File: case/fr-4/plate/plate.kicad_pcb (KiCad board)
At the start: 2 copper layers, 152.4 x 104.6 mm, 34 parts

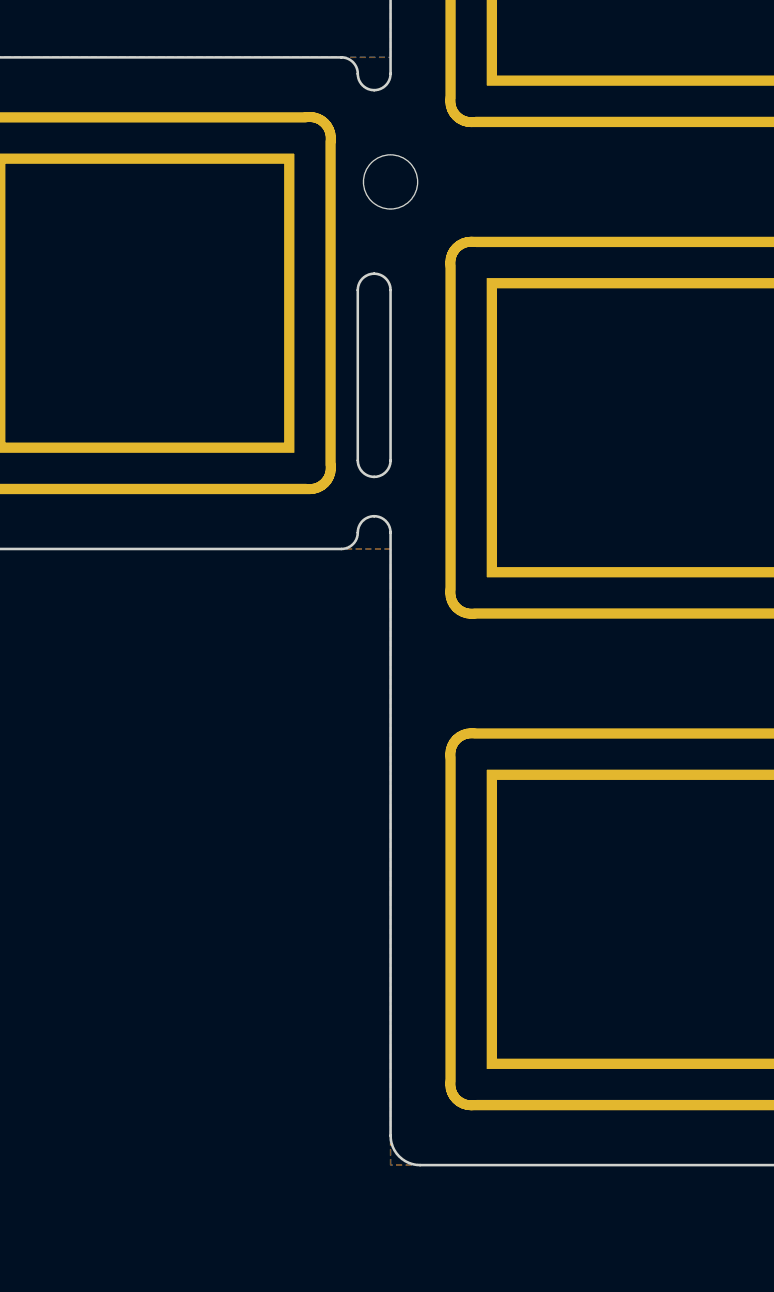
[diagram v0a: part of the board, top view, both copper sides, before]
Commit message: Edit cutout, re-fill zones
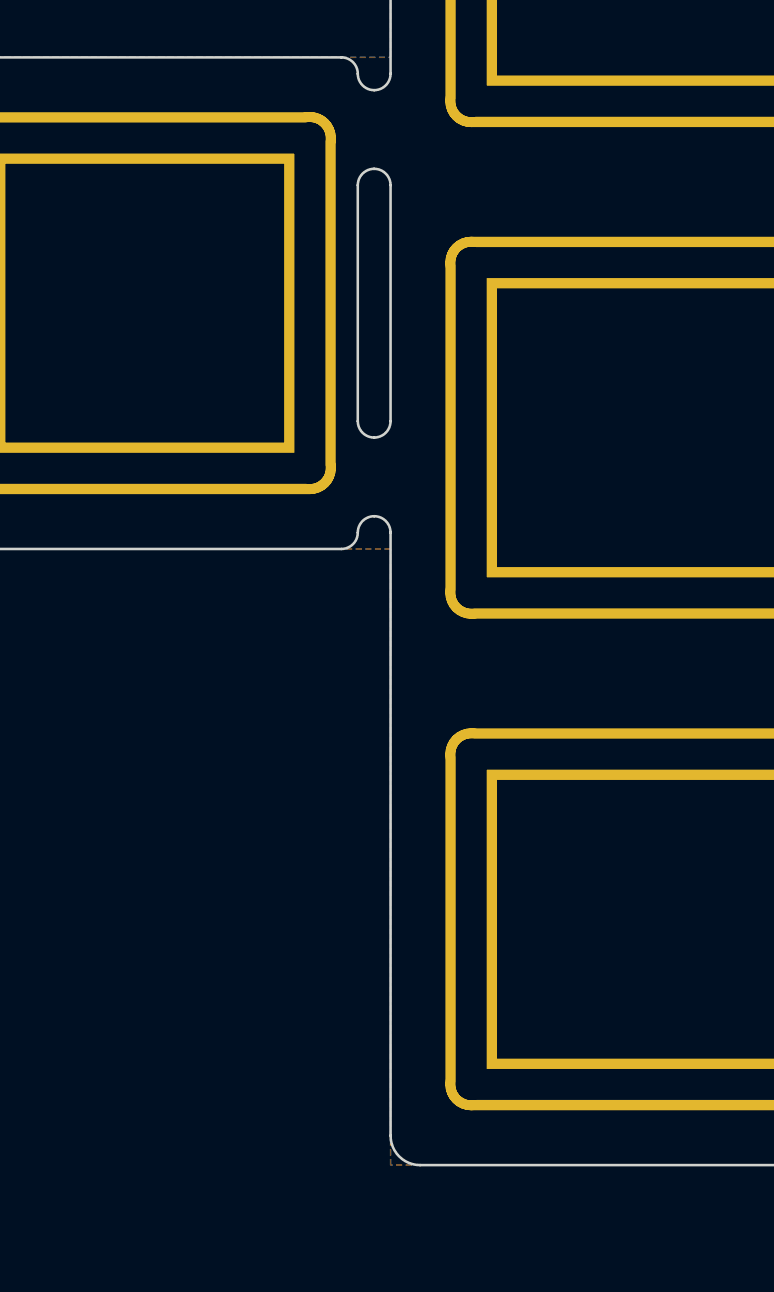
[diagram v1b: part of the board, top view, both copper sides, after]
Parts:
- removed H5: Hole_Mount_M2, jiran-ble-lite:Hole_Mount_M2
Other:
- outline, holes or cut-outs redrawn
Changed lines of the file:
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@@
     (pad "" thru_hole oval (at -6.4 0 270) (size 14.8 2) (drill oval 14 1.2) (layers *.Cu *.Mask))
-  )
-  (footprint "jiran-ble-lite:Hole_Mount_M2" (layer "F.Cu")
-    (at 89.027 100.965)
-    (fp_text reference "H5" (at 0 0 unlocked) (layer "F.SilkS") hide
-      (effects (font (size 1 1) (thickness 0.15)))
-    )
-    (fp_text value "Hole_Mount_M2" (at 0 2.65 unlocked) (layer "F.Fab") hide
-      (effects (font (size 1 1) (thickness 0.15)))
-    )
-    (fp_circle (center 0 0) (end 1.5 0) (layer "Cmts.User") (width 0.12) (fill none))
-    (pad "" np_thru_hole circle (at 0 0) (size 2.1 2.1) (drill 2.1) (layers *.Cu *.Mask))
   )
   (footprint "jiran-ble-lite:Mx_Cutout_1u" (layer "F.Cu")
@@
   (gr_line (start 165.227 49.784) (end 165.227 52.324) (layer "Edge.Cuts") (width 0.1))
   (gr_arc (start 125.984 59.436) (end 125.984 60.579) (angle -90) (layer "Edge.Cuts") (width 0.1))
+  (gr_arc (start 88.391992 96.774) (end 88.391992 97.408996) (angle 90) (layer "Edge.Cuts") (width 0.1))
   (gr_line (start 145.034 129.667) (end 128.27 129.667) (layer "Edge.Cuts") (width 0.1))
   (gr_line (start 109.22 60.579) (end 125.984 60.579) (layer "Edge.Cuts") (width 0.1))
   (gr_arc (start 166.37 147.574) (end 165.227 147.574) (angle -90) (layer "Edge.Cuts") (width 0.1))
-  (gr_arc (start 88.392 105.156) (end 88.392 104.521004) (angle 90) (layer "Edge.Cuts") (width 0.1))
   (gr_arc (start 183.134 54.61) (end 184.277 54.61) (angle -90) (layer "Edge.Cuts") (width 0.1))
   (gr_arc (start 164.084 49.784) (end 165.227 49.784) (angle -90) (layer "Edge.Cuts") (width 0.1))
@@
   (gr_arc (start 128.27 130.81) (end 128.27 129.667) (angle -90) (layer "Edge.Cuts") (width 0.1))
   (gr_line (start 127.127 59.436) (end 127.127 54.61) (layer "Edge.Cuts") (width 0.1))
-  (gr_line (start 89.026996 111.760004) (end 89.026996 105.156) (layer "Edge.Cuts") (width 0.1))
+  (gr_line (start 87.757004 101.091996) (end 87.757004 110.236004) (layer "Edge.Cuts") (width 0.1))
   (gr_line (start 183.134 148.717) (end 166.37 148.717) (layer "Edge.Cuts") (width 0.1))
+  (gr_arc (start 88.392 101.091996) (end 87.757004 101.091996) (angle 90) (layer "Edge.Cuts") (width 0.1))
   (gr_line (start 202.184 151.003) (end 185.42 151.003) (layer "Edge.Cuts") (width 0.1))
+  (gr_arc (start 87.122 96.774) (end 87.122 96.139004) (angle 90) (layer "Edge.Cuts") (width 0.1))
   (gr_arc (start 145.034 52.324) (end 145.034 53.467) (angle -90) (layer "Edge.Cuts") (width 0.1))
-  (gr_arc (start 88.391991 114.554005) (end 88.391991 113.919009) (angle 90) (layer "Edge.Cuts") (width 0.1))
+  (gr_arc (start 88.391992 114.554004) (end 87.756996 114.554004) (angle 90) (layer "Edge.Cuts") (width 0.1))
   (gr_arc (start 147.32 49.784) (end 147.32 48.641) (angle -90) (layer "Edge.Cuts") (width 0.1))
   (gr_line (start 166.37 53.467) (end 183.134 53.467) (layer "Edge.Cuts") (width 0.1))
-  (gr_arc (start 88.392 111.760004) (end 89.026996 111.760004) (angle 90) (layer "Edge.Cuts") (width 0.1))
   (gr_arc (start 90.17 137.922) (end 89.027 137.922) (angle -90) (layer "Edge.Cuts") (width 0.1))
   (gr_line (start 69.977 114.046) (end 69.977 97.282) (layer "Edge.Cuts") (width 0.1))
   (gr_arc (start 185.42 149.86) (end 184.277 149.86) (angle -90) (layer "Edge.Cuts") (width 0.1))
   (gr_arc (start 202.184 56.896) (end 203.327 56.896) (angle -90) (layer "Edge.Cuts") (width 0.1))
-  (gr_arc (start 88.391992 96.774) (end 88.391992 97.408996) (angle 90) (layer "Edge.Cuts") (width 0.1))
   (gr_arc (start 185.42 54.61) (end 184.277 54.61) (angle -90) (layer "Edge.Cuts") (width 0.1))
   (gr_line (start 146.177 125.984) (end 146.177 128.524) (layer "Edge.Cuts") (width 0.1))
@@
   (gr_line (start 146.177 52.324) (end 146.177 49.784) (layer "Edge.Cuts") (width 0.1))
   (gr_arc (start 183.134 149.86) (end 184.277 149.86) (angle -90) (layer "Edge.Cuts") (width 0.1))
-  (gr_line (start 89.027 64.008) (end 89.026989 96.773999) (layer "Edge.Cuts") (width 0.1))
+  (gr_arc (start 88.392 101.091996) (end 88.392 100.457) (angle 90) (layer "Edge.Cuts") (width 0.1))
   (gr_arc (start 128.27 54.61) (end 128.27 53.467) (angle -90) (layer "Edge.Cuts") (width 0.1))
   (gr_arc (start 125.984 135.636) (end 125.984 136.779) (angle -90) (layer "Edge.Cuts") (width 0.1))
@@
   (gr_line (start 222.377 135.382) (end 222.377 152.146) (layer "Edge.Cuts") (width 0.1))
   (gr_arc (start 109.22 61.722) (end 109.22 60.579) (angle -90) (layer "Edge.Cuts") (width 0.1))
+  (gr_line (start 89.026988 114.554004) (end 89.027 137.922) (layer "Edge.Cuts") (width 0.1))
   (gr_arc (start 71.12 114.046) (end 69.977 114.046) (angle -90) (layer "Edge.Cuts") (width 0.1))
   (gr_arc (start 147.32 125.984) (end 147.32 124.841) (angle -90) (layer "Edge.Cuts") (width 0.1))
-  (gr_line (start 87.757004 105.156) (end 87.757004 111.760004) (layer "Edge.Cuts") (width 0.1))
   (gr_arc (start 106.934 137.922) (end 106.934 139.065) (angle -90) (layer "Edge.Cuts") (width 0.1))
   (gr_arc (start 109.22 137.922) (end 109.22 136.779) (angle -90) (layer "Edge.Cuts") (width 0.1))
+  (gr_arc (start 88.392 110.236004) (end 88.392 110.871) (angle 90) (layer "Edge.Cuts") (width 0.1))
   (gr_line (start 106.934 139.065) (end 90.17 139.065) (layer "Edge.Cuts") (width 0.1))
-  (gr_arc (start 88.391993 96.773999) (end 89.026989 96.773999) (angle 90) (layer "Edge.Cuts") (width 0.1))
   (gr_arc (start 204.47 133.096) (end 203.327 133.096) (angle -90) (layer "Edge.Cuts") (width 0.1))
   (gr_line (start 147.32 48.641) (end 164.084 48.641) (layer "Edge.Cuts") (width 0.1))
@@
   (gr_line (start 164.084 124.841) (end 147.32 124.841) (layer "Edge.Cuts") (width 0.1))
   (gr_arc (start 106.934 61.722) (end 106.934 62.865) (angle -90) (layer "Edge.Cuts") (width 0.1))
-  (gr_arc (start 88.392 111.760004) (end 88.392 112.395) (angle 90) (layer "Edge.Cuts") (width 0.1))
-  (gr_arc (start 88.391992 114.554004) (end 87.756996 114.554004) (angle 90) (layer "Edge.Cuts") (width 0.1))
   (gr_arc (start 145.034 128.524) (end 145.034 129.667) (angle -90) (layer "Edge.Cuts") (width 0.1))
   (gr_arc (start 166.37 52.324) (end 165.227 52.324) (angle -90) (layer "Edge.Cuts") (width 0.1))
   (gr_line (start 165.227 147.574) (end 165.227 125.984) (layer "Edge.Cuts") (width 0.1))
   (gr_arc (start 221.234 152.146) (end 221.234 153.289) (angle -90) (layer "Edge.Cuts") (width 0.1))
+  (gr_arc (start 88.392 110.236004) (end 89.026996 110.236004) (angle 90) (layer "Edge.Cuts") (width 0.1))
+  (gr_arc (start 88.391992 114.554004) (end 88.391992 113.919008) (angle 90) (layer "Edge.Cuts") (width 0.1))
   (gr_arc (start 71.12 97.282) (end 71.12 96.139) (angle -90) (layer "Edge.Cuts") (width 0.1))
   (gr_arc (start 204.47 152.146) (end 203.327 152.146) (angle -90) (layer "Edge.Cuts") (width 0.1))
   (gr_arc (start 90.17 64.008) (end 90.17 62.865) (angle -90) (layer "Edge.Cuts") (width 0.1))
+  (gr_line (start 89.026996 110.236004) (end 89.026996 101.091996) (layer "Edge.Cuts") (width 0.1))
+  (gr_arc (start 87.122 114.554004) (end 87.756996 114.554004) (angle 90) (layer "Edge.Cuts") (width 0.1))
   (gr_line (start 71.12 96.139) (end 87.122 96.139004) (layer "Edge.Cuts") (width 0.1))
-  (gr_arc (start 87.122 114.554004) (end 87.756996 114.554004) (angle 90) (layer "Edge.Cuts") (width 0.1))
-  (gr_line (start 89.027 137.922) (end 89.026987 114.554005) (layer "Edge.Cuts") (width 0.1))
-  (gr_arc (start 87.122 96.774) (end 87.122 96.139004) (angle 90) (layer "Edge.Cuts") (width 0.1))
-  (gr_arc (start 88.392 105.156) (end 87.757004 105.156) (angle 90) (layer "Edge.Cuts") (width 0.1))
+  (gr_line (start 89.027 64.008) (end 89.026989 96.773999) (layer "Edge.Cuts") (width 0.1))
   (gr_line (start 203.327 56.896) (end 203.327 133.096) (layer "Edge.Cuts") (width 0.1))
+  (gr_arc (start 88.391993 96.773999) (end 89.026989 96.773999) (angle 90) (layer "Edge.Cuts") (width 0.1))
   (zone (net 0) (net_name "") (layer "F.Cu") (hatch edge 0.508)
     (connect_pads (clearance 0.508))
